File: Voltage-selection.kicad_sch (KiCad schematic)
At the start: 15 parts, among them Q3 DMP1045U-7, Q4 DMP1045U-7, Q5 DMP1045U-7, SW4 12V 50mA

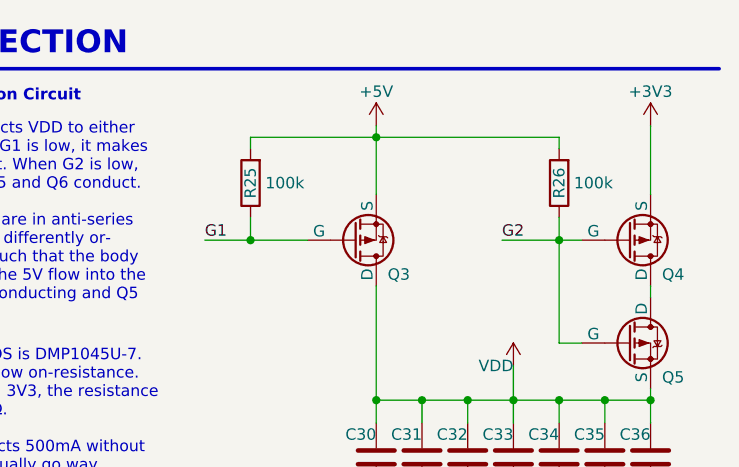
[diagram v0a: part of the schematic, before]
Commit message: Rename 'modify_designators.py' into 'kicad_designators.py'
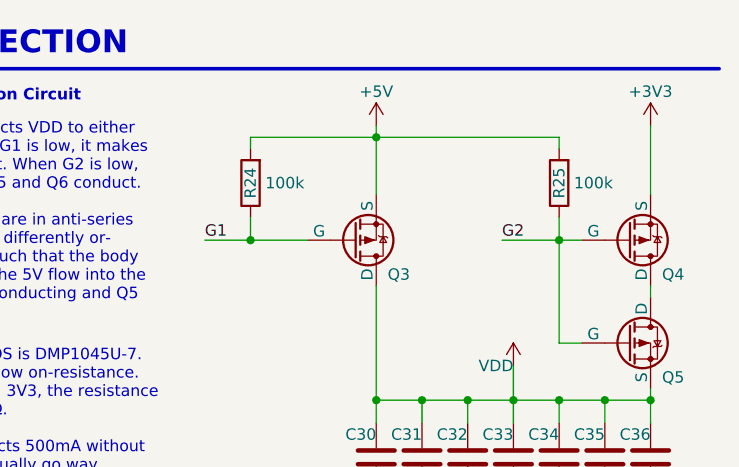
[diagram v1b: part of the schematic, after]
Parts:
- renumbered R25 to R24, R26 to R25
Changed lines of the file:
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@@
   (symbol (lib_id "Device:R") (at 144.78 31.75 180) (unit 1)
     (in_bom yes) (on_board yes) (dnp no)
-    (property "Reference" "R25" (at 144.78 31.75 90)
+    (property "Reference" "R24" (at 144.78 31.75 90)
       (effects (font (size 1.27 1.27)))
     )
@@
       (project "tiny-scarab"
         (path "/156c5422-ee07-49a4-8263-a2dbd26b90bd/481ed0a2-b40b-451f-8f8b-138317026240"
-          (reference "R25") (unit 1)
+          (reference "R24") (unit 1)
         )
       )
@@
   (symbol (lib_id "Device:R") (at 179.07 31.75 180) (unit 1)
     (in_bom yes) (on_board yes) (dnp no)
-    (property "Reference" "R26" (at 179.07 31.75 90)
+    (property "Reference" "R25" (at 179.07 31.75 90)
       (effects (font (size 1.27 1.27)))
     )
@@
       (project "tiny-scarab"
         (path "/156c5422-ee07-49a4-8263-a2dbd26b90bd/481ed0a2-b40b-451f-8f8b-138317026240"
-          (reference "R26") (unit 1)
-        )
-      )
+          (reference "R25") (unit 1)
+        )
+      )

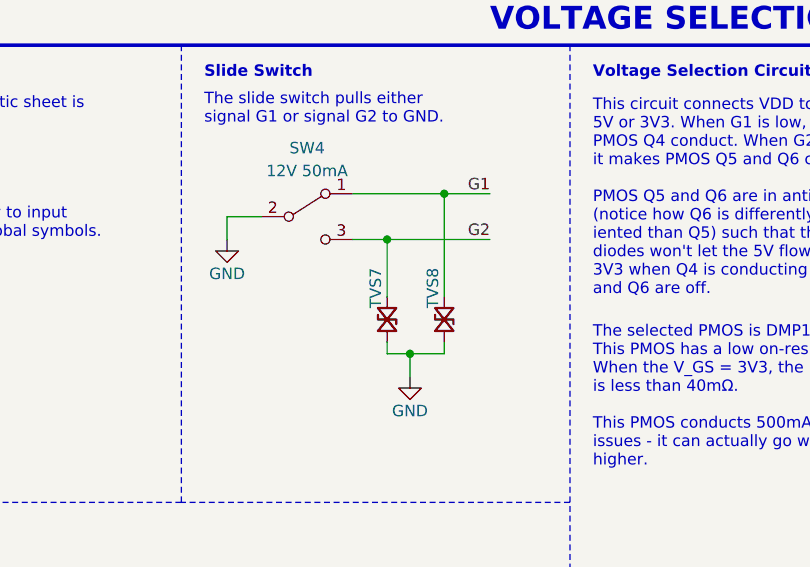
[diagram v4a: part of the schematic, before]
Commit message: Replace TVS `SP1007-01ETG` with `LESD8LH5.0CT5G`
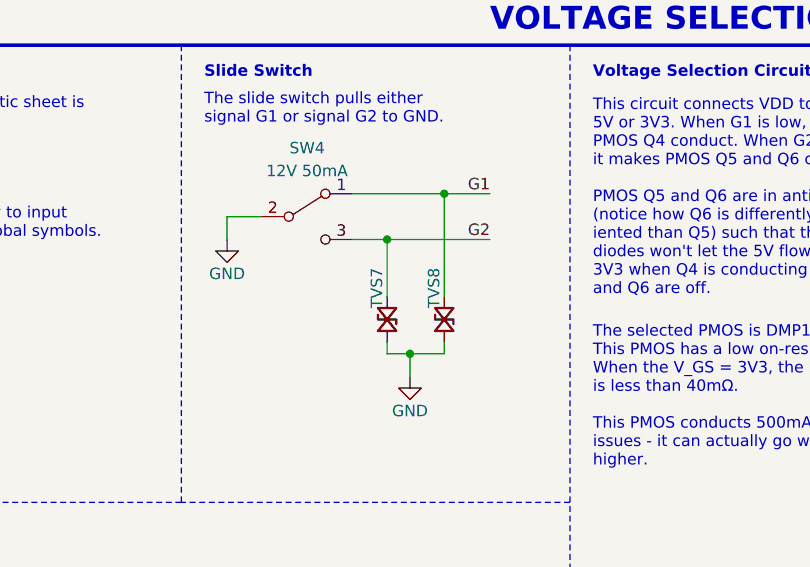
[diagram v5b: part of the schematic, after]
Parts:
- removed TVS7, TVS8: 5V, Tiny_Scarab:D_SOD-882_SP1007-01ETG, symbol Tiny_Scarab:TVS_SP1007-01ETG
- added TVS7, TVS8: 5V, Tiny_Scarab:D_SOD-882_SP1007-01ETG, symbol Tiny_Scarab:TVS_LESD8LH5.0CT5G
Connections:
- net G1: now also TVS8.1
- net G2: now also TVS7.1
- net GND: now also TVS7.2, TVS8.2
